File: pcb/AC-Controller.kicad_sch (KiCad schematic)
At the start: 33 parts, among them J1 Serial, Q1 AO3400A, SW1 Mode, SW2 Value, SW3 RESET, U1 ESP32-WROOM-32

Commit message: feat: replace contrast pot with more common type
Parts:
- RV1: footprint Potentiometer_SMD:Potentiometer_Bourns_3224J_Horizontal -> Potentiometer_THT:Potentiometer_Runtron_RM-065_Vertical
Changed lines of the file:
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@@
       (effects (font (size 1.27 1.27)) (justify right))
     )
-    (property "Footprint" "Potentiometer_SMD:Potentiometer_Bourns_3224J_Horizontal" (at 246.38 107.95 0)
+    (property "Footprint" "Potentiometer_THT:Potentiometer_Runtron_RM-065_Vertical" (at 246.38 107.95 0)
       (effects (font (size 1.27 1.27)) hide)
     )

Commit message: feat: replace TP4056 Prog Resistor footprint with 0603
Replace the footprint for the programming resistor to 0603 to make replacing it easier. Also changing the default value to 4.7k for slower charge and less heat production
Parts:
- R8: footprint Resistor_SMD:R_0603_1608Metric -> Resistor_SMD:R_0603_1608Metric_Pad0.98x0.95mm_HandSolder
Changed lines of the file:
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@@
       (effects (font (size 1.27 1.27)))
     )
-    (property "Footprint" "Resistor_SMD:R_0603_1608Metric" (at 209.55 118.11 0)
+    (property "Footprint" "Resistor_SMD:R_0603_1608Metric_Pad0.98x0.95mm_HandSolder" (at 209.55 118.11 0)
       (effects (font (size 1.27 1.27)) hide)
     )

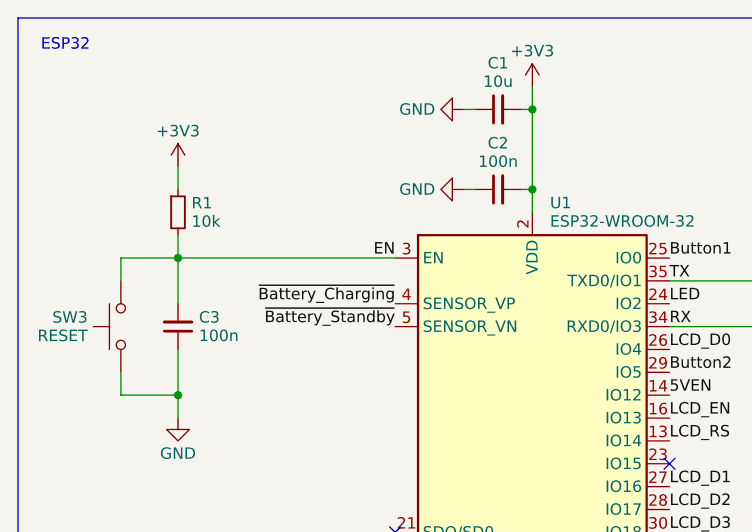
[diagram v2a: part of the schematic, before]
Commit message: feat: add disable jumper for battery charger
Adding a jumper to disable the TP4056 Battery Charger IC in case no battery is connected and the device is powered by USB only. No need for the IC to draw power in that case.
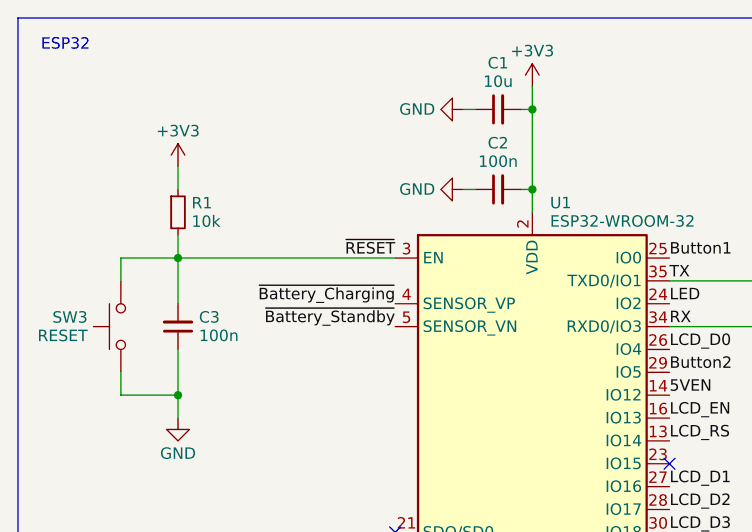
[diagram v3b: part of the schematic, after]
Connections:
- net EN renamed ~{RESET}
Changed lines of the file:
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@@
     (effects (font (size 1.27 1.27)) (justify right bottom))
   )
-  (label "EN" (at 62.23 45.72 180) (fields_autoplaced)
+  (label "~{RESET}" (at 62.23 45.72 180) (fields_autoplaced)
     (effects (font (size 1.27 1.27)) (justify right bottom))
   )

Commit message: style: board and schematics cleanup
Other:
- note added: "Power Supply"
- moved on the sheet: C13, C4, C5, C6, C7, R2, R24, R25, R28, R3, R4, R5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

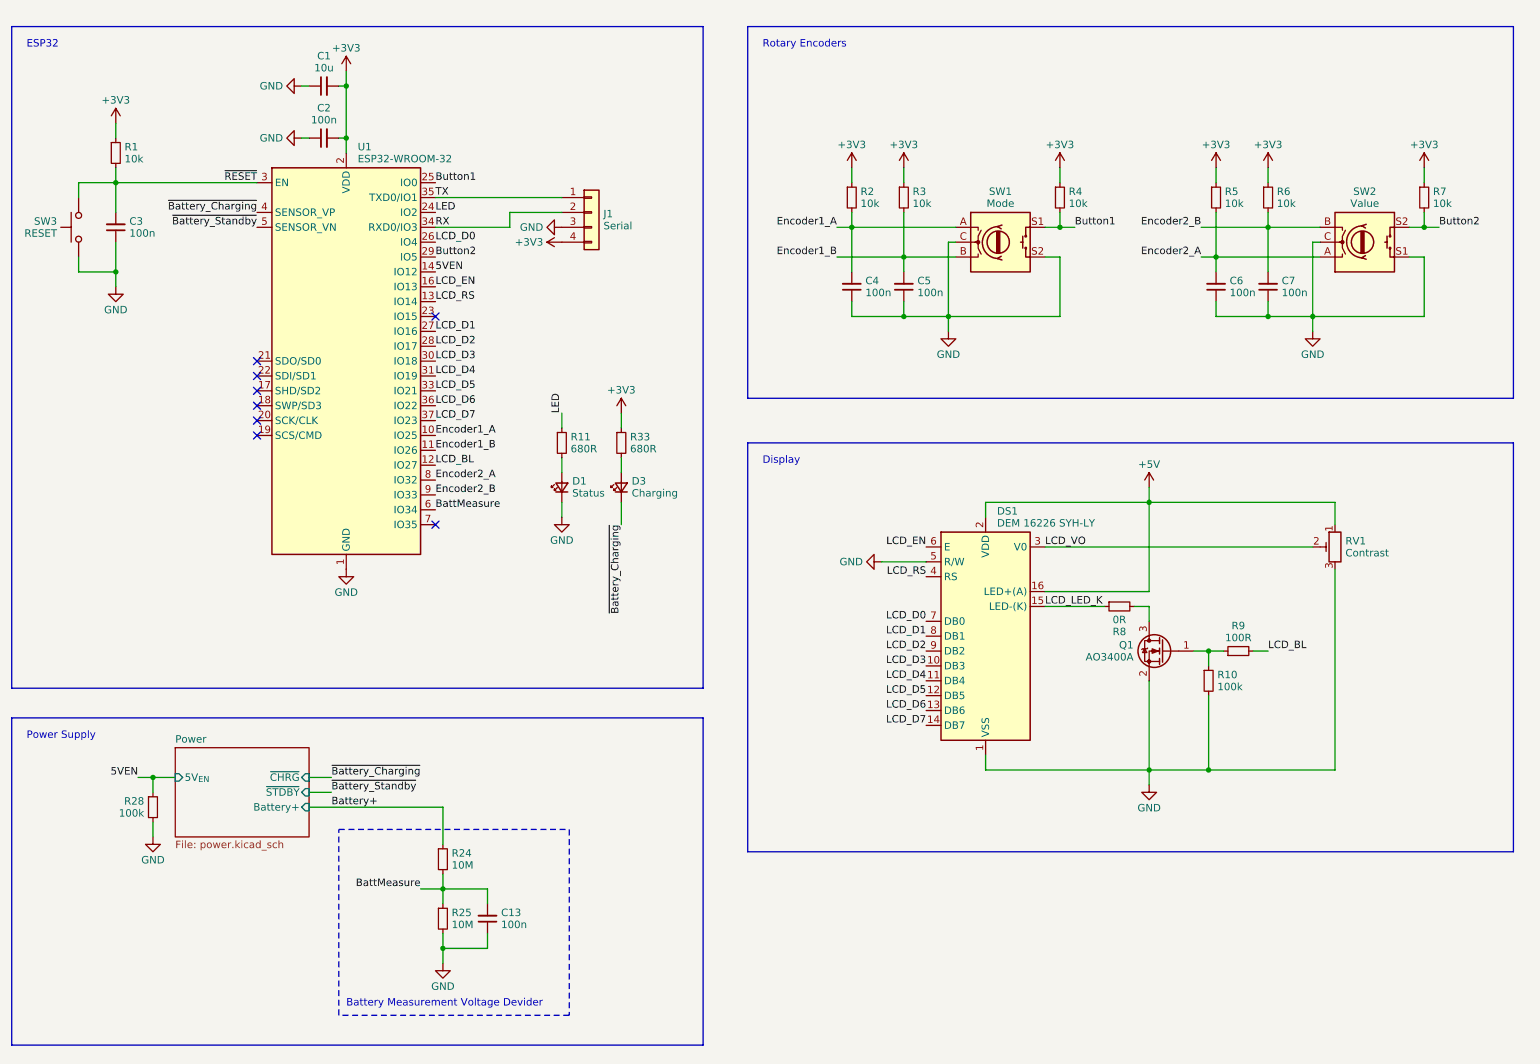
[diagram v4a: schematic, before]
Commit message: feat: add more ways to wake up
Adding simple MOSFET logic to watch 4 signals for waking up from deep sleep
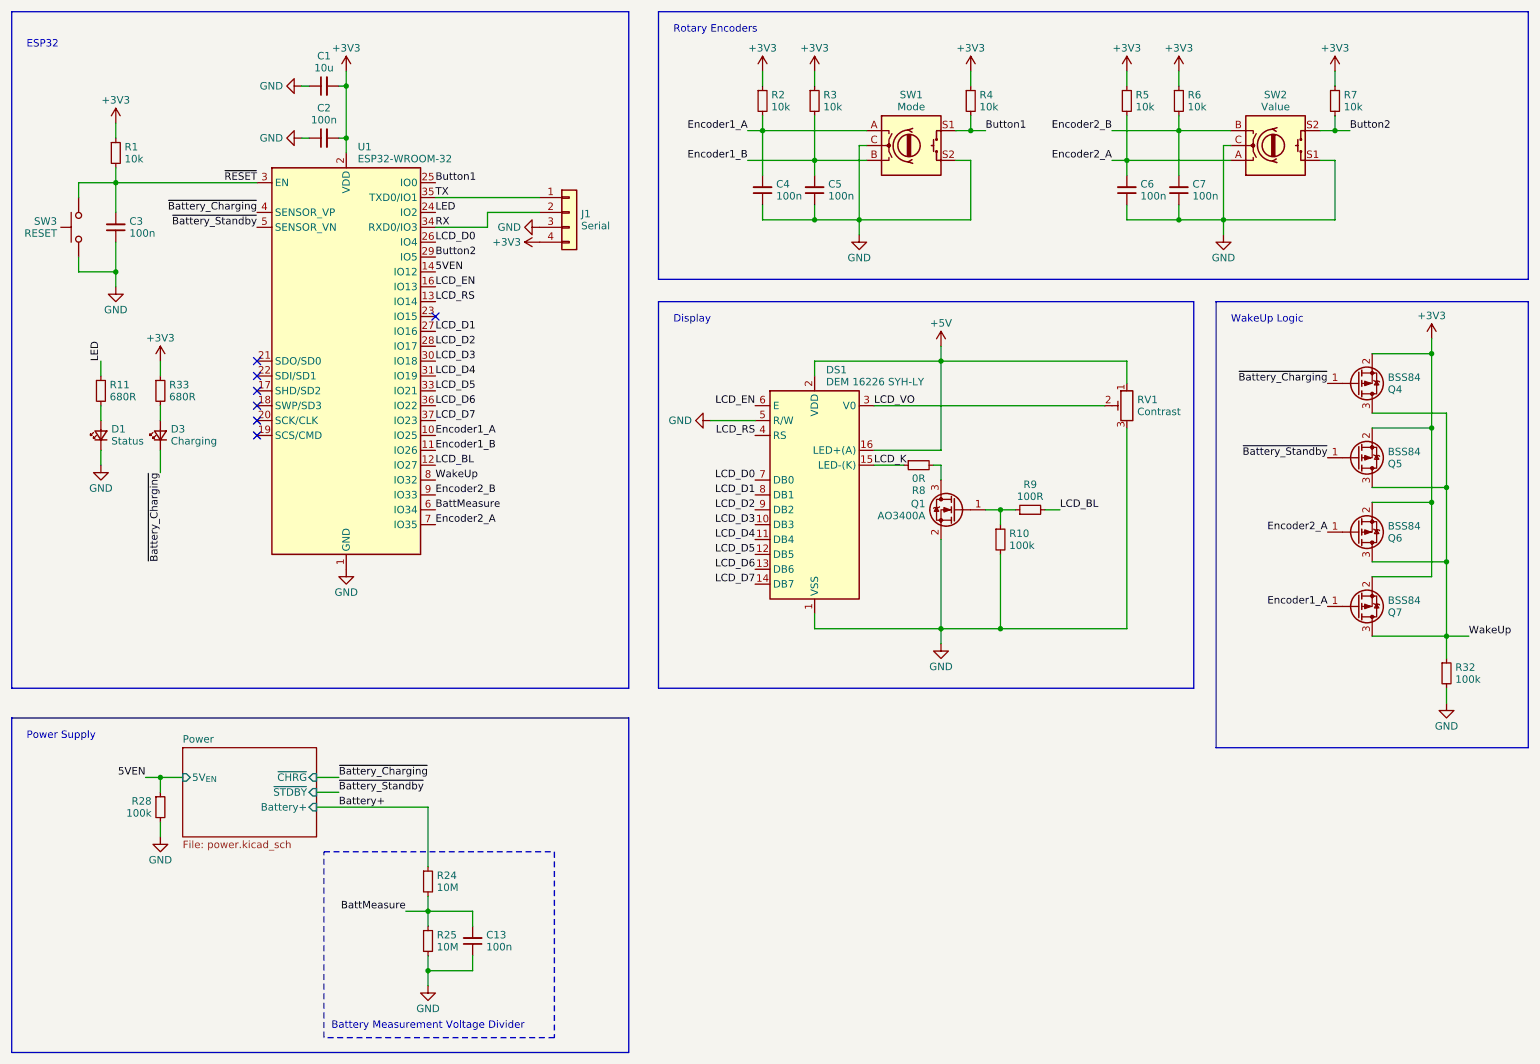
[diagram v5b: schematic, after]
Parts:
- added Q4, Q5, Q6, Q7: BSS84, Package_TO_SOT_SMD:SOT-23, symbol Transistor_FET:BSS84
- added R32: 100k, Resistor_SMD:R_0402_1005Metric, symbol Device:R_Small
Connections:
- net +3V3: now also Q4.2 (S), Q5.2 (S), Q6.2 (S), Q7.2 (S)
- net Encoder1_A: now also Q7.1 (G)
- net Encoder2_A: now also U1.7 (IO35), Q6.1 (G); no longer U1.8 (IO32)
- net GND: now also R32.2
- net ~{Battery_Charging}: now also Q4.1 (G)
- net ~{Battery_Standby}: now also Q5.1 (G)
- net LCD_LED_K renamed LCD_K
- new net WakeUp: Q4.3 (D), Q5.3 (D), Q6.3 (D), Q7.3 (D), R32.1, U1.8 (IO32)
- no-connect marks 8 -> 7
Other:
- note added: "Battery Measurement Voltage Divider"
- note added: "WakeUp Logic"
- note removed: "Battery Measurement Voltage Devider"
- moved on the sheet: C13, C4, C5, C6, C7, D1, D3, DS1, J1, Q1, R10, R11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

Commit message: style: cleanup
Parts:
- renumbered Q4 to Q5, Q5 to Q6, Q6 to Q7, Q7 to Q8
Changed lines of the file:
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@@
   (symbol (lib_id "Transistor_FET:BSS84") (at 250.19 105.41 0) (mirror x) (unit 1)
     (in_bom yes) (on_board yes) (dnp no)
-    (property "Reference" "Q6" (at 255.397 106.434 0)
+    (property "Reference" "Q7" (at 255.397 106.434 0)
       (effects (font (size 1.27 1.27)) (justify left))
     )
@@
       (project "AC-Controller"
         (path "/a9b77c2b-ed0c-4412-867d-4d65898d0fc4"
-          (reference "Q6") (unit 1)
+          (reference "Q7") (unit 1)
         )
       )
@@
   (symbol (lib_id "Transistor_FET:BSS84") (at 250.19 92.71 0) (mirror x) (unit 1)
     (in_bom yes) (on_board yes) (dnp no)
-    (property "Reference" "Q5" (at 255.397 93.734 0)
+    (property "Reference" "Q6" (at 255.397 93.734 0)
       (effects (font (size 1.27 1.27)) (justify left))
     )
@@
       (project "AC-Controller"
         (path "/a9b77c2b-ed0c-4412-867d-4d65898d0fc4"
-          (reference "Q5") (unit 1)
+          (reference "Q6") (unit 1)
         )
       )
@@
   (symbol (lib_id "Transistor_FET:BSS84") (at 250.19 118.11 0) (mirror x) (unit 1)
     (in_bom yes) (on_board yes) (dnp no)
-    (property "Reference" "Q7" (at 255.397 119.134 0)
+    (property "Reference" "Q8" (at 255.397 119.134 0)
       (effects (font (size 1.27 1.27)) (justify left))
     )
@@
       (project "AC-Controller"
         (path "/a9b77c2b-ed0c-4412-867d-4d65898d0fc4"
-          (reference "Q7") (unit 1)
+          (reference "Q8") (unit 1)
         )
       )
@@
   (symbol (lib_id "Transistor_FET:BSS84") (at 250.19 80.01 0) (mirror x) (unit 1)
     (in_bom yes) (on_board yes) (dnp no)
-    (property "Reference" "Q4" (at 255.397 81.034 0)
+    (property "Reference" "Q5" (at 255.397 81.034 0)
       (effects (font (size 1.27 1.27)) (justify left))
     )
@@
       (project "AC-Controller"
         (path "/a9b77c2b-ed0c-4412-867d-4d65898d0fc4"
-          (reference "Q4") (unit 1)
-        )
-      )
+          (reference "Q5") (unit 1)
+        )
+      )

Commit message: fix: add missing part numbers
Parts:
- Q5, Q6, Q7, Q8: LCSC (none) -> C8492
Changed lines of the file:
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@@
       (effects (font (size 1.27 1.27)) (justify left) hide)
+    )
+    (property "LCSC" "C8492" (at 250.19 105.41 0)
+      (effects (font (size 1.27 1.27)) hide)
     )
     (pin "1")
@@
     (property "Datasheet" "http://assets.nexperia.com/documents/data-sheet/BSS84.pdf" (at 250.19 92.71 0)
       (effects (font (size 1.27 1.27)) (justify left) hide)
+    )
+    (property "LCSC" "C8492" (at 250.19 92.71 0)
+      (effects (font (size 1.27 1.27)) hide)
     )
     (pin "1")
@@
       (effects (font (size 1.27 1.27)) (justify left) hide)
     )
+    (property "LCSC" "C8492" (at 250.19 118.11 0)
+      (effects (font (size 1.27 1.27)) hide)
+    )
     (pin "1")
     (pin "2")
@@
       (effects (font (size 1.27 1.27)) (justify left) hide)
     )
-    (pin "1")
+    (property "LCSC" "C8492" (at 250.19 80.01 0)
+      (effects (font (size 1.27 1.27)) hide)
+    )
+    (pin "1")
